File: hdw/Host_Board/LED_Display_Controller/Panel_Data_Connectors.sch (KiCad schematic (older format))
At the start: 4 parts

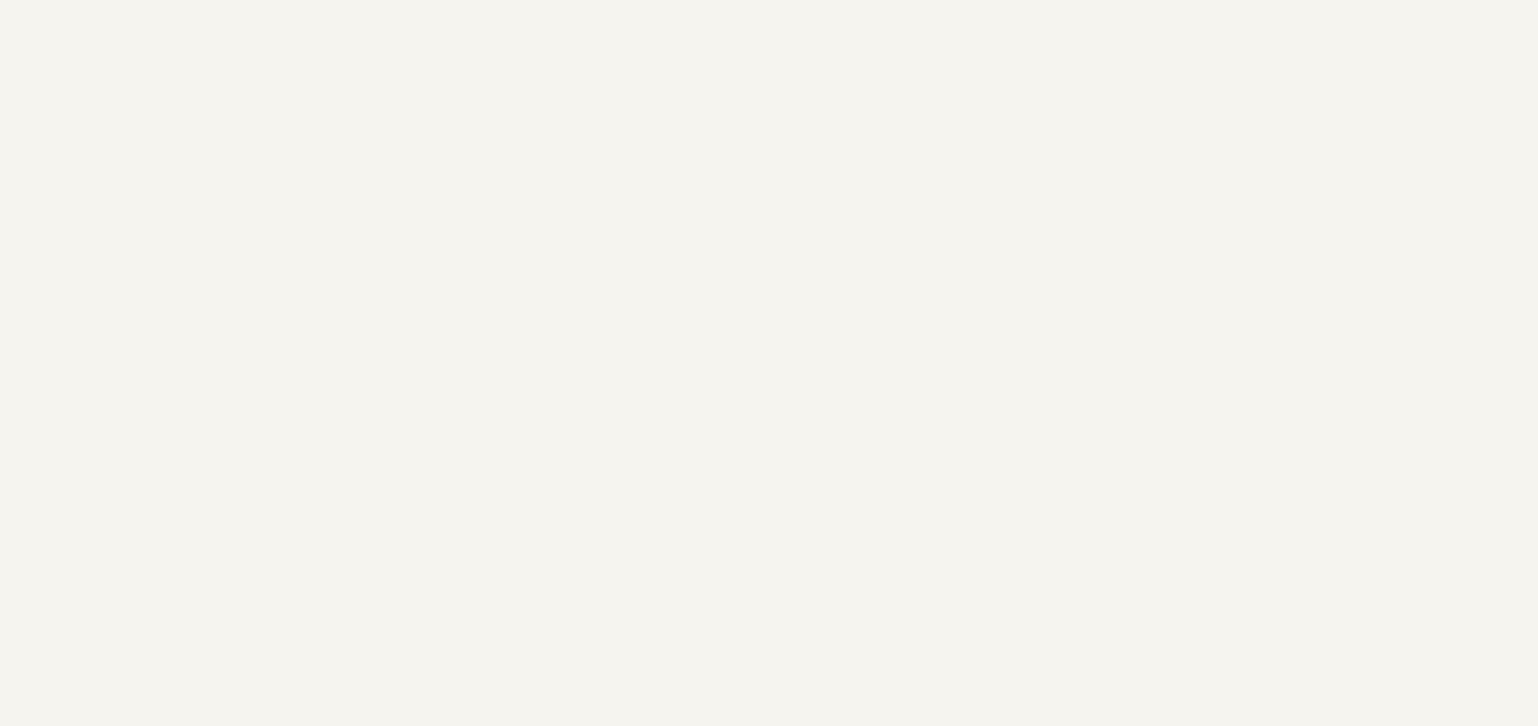
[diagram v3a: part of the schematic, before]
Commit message: Added graphical symbols to certain sheets
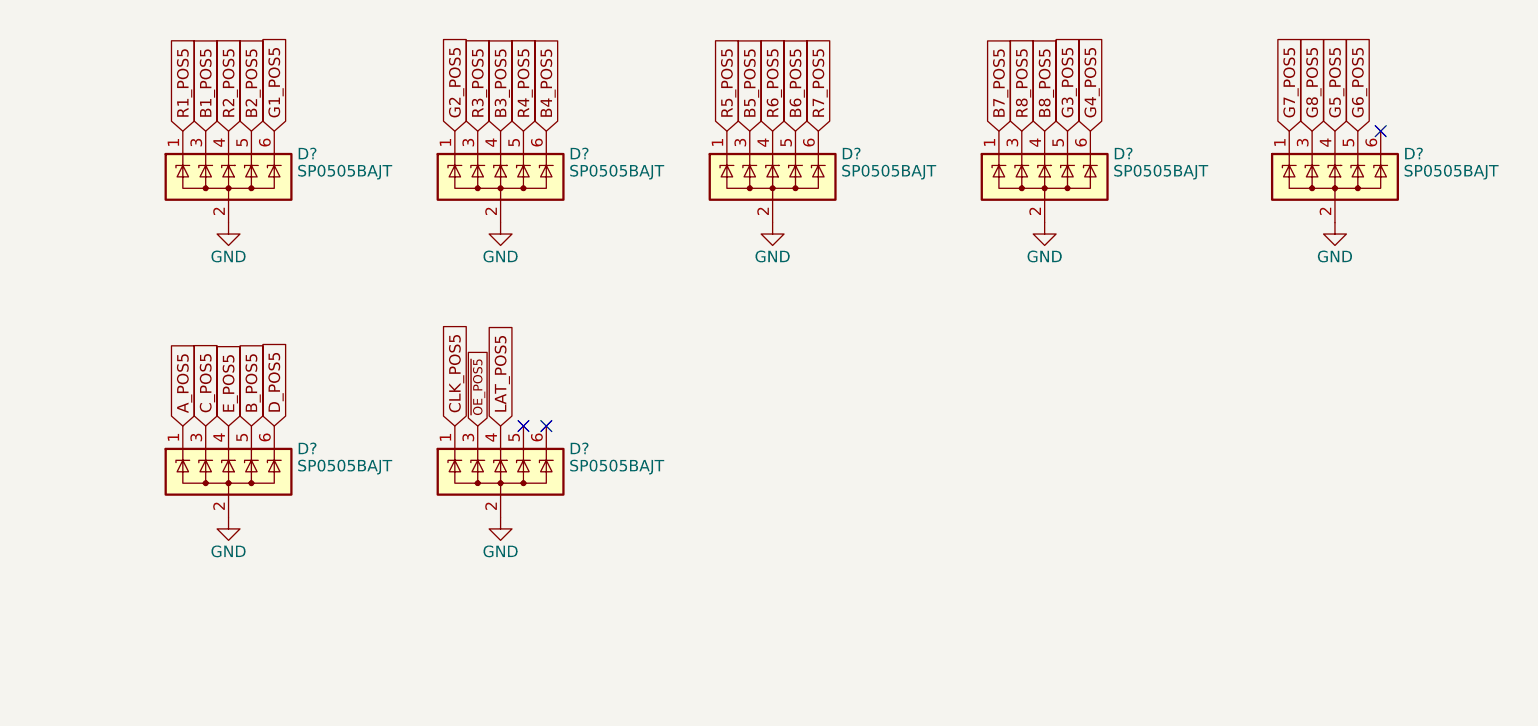
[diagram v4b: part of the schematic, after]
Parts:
- added D? (x7): SP0505BAJT, Package_TO_SOT_SMD:SOT-363_SC-70-6, symbol Power_Protection:SP0505BAJT
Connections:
- net A_POS5: now also D?.1 (K)
- net B1_POS5: now also D?.3 (K)
- net B2_POS5: now also D?.5 (K)
- net B3_POS5: now also D?.4 (K)
- net B4_POS5: now also D?.6 (K)
- net B5_POS5: now also D?.3 (K)
- net B6_POS5: now also D?.5 (K)
- net B7_POS5: now also D?.1 (K)
- net B8_POS5: now also D?.4 (K)
- net B_POS5: now also D?.5 (K)
- net CLK_POS5: now also D?.1 (K)
- net C_POS5: now also D?.3 (K)
- net D_POS5: now also D?.6 (K)
- net E_POS5: now also D?.4 (K)
- net G1_POS5: now also D?.6 (K)
- net G2_POS5: now also D?.1 (K)
- net G3_POS5: now also D?.5 (K)
- net G4_POS5: now also D?.6 (K)
- net G5_POS5: now also D?.4 (K)
- net G6_POS5: now also D?.5 (K)
- net G7_POS5: now also D?.1 (K)
- net G8_POS5: now also D?.3 (K)
- net GND: now also D?.2 (A), D?.2 (A), D?.2 (A), D?.2 (A), D?.2 (A), D?.2 (A), D?.2 (A)
- net LAT_POS5: now also D?.4 (K)
- net R1_POS5: now also D?.1 (K)
- net R2_POS5: now also D?.4 (K)
- net R3_POS5: now also D?.3 (K)
- net R4_POS5: now also D?.5 (K)
- net R5_POS5: now also D?.1 (K)
- net R6_POS5: now also D?.4 (K)
- net R7_POS5: now also D?.6 (K)
- net R8_POS5: now also D?.3 (K)
- net ~OE_POS5: now also D?.3 (K)
- no-connect marks 0 -> 3
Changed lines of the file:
@@
 	3400 6100 3400 6700
 Connection ~ 3400 6700
+$Comp
+L Power_Protection:SP0505BAJT D?
+U 1 1 5BFD0D17
+P 5000 1680
+F 0 "D?" H 5300 1780 50  0000 L CNN
+F 1 "SP0505BAJT" H 5300 1705 50  0000 L CNN
+F 2 "Package_TO_SOT_SMD:SOT-363_SC-70-6" H 5300 1630 50  0001 L CNN
+F 3 "http://www.littelfuse.com/~/media/files/littelfuse/technical%20resources/documents/data%20sheets/sp05xxba.pdf" H 5125 1805 50  0001 C CNN
+	1    5000 1680
+	1    0    0    -1
+$EndComp
+Text GLabel 4800 2770 1    50   Input ~ 0
+A_POS5
+Text GLabel 4900 2770 1    50   Input ~ 0
+C_POS5
+Text GLabel 4800 1480 1    50   Input ~ 0
+R1_POS5
+Text GLabel 4900 1480 1    50   Input ~ 0
+B1_POS5
+Text GLabel 5000 1480 1    50   Input ~ 0
+R2_POS5
+Text GLabel 5100 1480 1    50   Input ~ 0
+B2_POS5
+Text GLabel 5990 2770 1    50   Input ~ 0
+CLK_POS5
+Text GLabel 6090 2770 1    40   Input ~ 0
+~OE_POS5
+Text GLabel 5100 2770 1    50   Input ~ 0
+B_POS5
+Text GLabel 5200 2770 1    50   Input ~ 0
+D_POS5
+Text GLabel 5000 2770 1    50   Input ~ 0
+E_POS5
+Text GLabel 6190 2770 1    50   Input ~ 0
+LAT_POS5
+Text GLabel 5200 1480 1    50   Input ~ 0
+G1_POS5
+Text GLabel 5990 1480 1    50   Input ~ 0
+G2_POS5
+Text GLabel 6090 1480 1    50   Input ~ 0
+R3_POS5
+Text GLabel 6190 1480 1    50   Input ~ 0
+B3_POS5
+Text GLabel 6290 1480 1    50   Input ~ 0
+R4_POS5
+Text GLabel 6390 1480 1    50   Input ~ 0
+B4_POS5
+Text GLabel 7180 1480 1    50   Input ~ 0
+R5_POS5
+Text GLabel 7280 1480 1    50   Input ~ 0
+B5_POS5
+Text GLabel 7380 1480 1    50   Input ~ 0
+R6_POS5
+Text GLabel 7480 1480 1    50   Input ~ 0
+B6_POS5
+Text GLabel 7580 1480 1    50   Input ~ 0
+R7_POS5
+Text GLabel 8370 1480 1    50   Input ~ 0
+B7_POS5
+Text GLabel 8470 1480 1    50   Input ~ 0
+R8_POS5
+Text GLabel 8570 1480 1    50   Input ~ 0
+B8_POS5
+Text GLabel 8670 1480 1    50   Input ~ 0
+G3_POS5
+Text GLabel 8770 1480 1    50   Input ~ 0
+G4_POS5
+Text GLabel 9840 1480 1    50   Input ~ 0
+G5_POS5
+Text GLabel 9940 1480 1    50   Input ~ 0
+G6_POS5
+Text GLabel 9640 1480 1    50   Input ~ 0
+G7_POS5
+Text GLabel 9740 1480 1    50   Input ~ 0
+G8_POS5
+$Comp
+L power:GND #PWR?
+U 1 1 5BFE01B1
+P 5000 1880
+F 0 "#PWR?" H 5000 1630 50  0001 C CNN
+F 1 "GND" H 5000 1730 50  0000 C CNN
+F 2 "" H 5000 1880 50  0001 C CNN
+F 3 "" H 5000 1880 50  0001 C CNN
+	1    5000 1880
+	1    0    0    -1
+$EndComp
+$Comp
+L Power_Protection:SP0505BAJT D?
+U 1 1 5BFE2189
+P 6190 1680
+F 0 "D?" H 6490 1780 50  0000 L CNN
+F 1 "SP0505BAJT" H 6490 1705 50  0000 L CNN
+F 2 "Package_TO_SOT_SMD:SOT-363_SC-70-6" H 6490 1630 50  0001 L CNN
+F 3 "http://www.littelfuse.com/~/media/files/littelfuse/technical%20resources/documents/data%20sheets/sp05xxba.pdf" H 6315 1805 50  0001 C CNN
+	1    6190 1680
+	1    0    0    -1
+$EndComp
+$Comp
+L power:GND #PWR?
+U 1 1 5BFE2190
+P 6190 1880
+F 0 "#PWR?" H 6190 1630 50  0001 C CNN
+F 1 "GND" H 6190 1730 50  0000 C CNN
+F 2 "" H 6190 1880 50  0001 C CNN
+F 3 "" H 6190 1880 50  0001 C CNN
+	1    6190 1880
+	1    0    0    -1
+$EndComp
+$Comp
+L Power_Protection:SP0505BAJT D?
+U 1 1 5BFE454E
+P 7380 1680
+F 0 "D?" H 7680 1780 50  0000 L CNN
+F 1 "SP0505BAJT" H 7680 1705 50  0000 L CNN
+F 2 "Package_TO_SOT_SMD:SOT-363_SC-70-6" H 7680 1630 50  0001 L CNN
+F 3 "http://www.littelfuse.com/~/media/files/littelfuse/technical%20resources/documents/data%20sheets/sp05xxba.pdf" H 7505 1805 50  0001 C CNN
+	1    7380 1680
+	1    0    0    -1
+$EndComp
+$Comp
+L power:GND #PWR?
+U 1 1 5BFE4555
+P 7380 1880
+F 0 "#PWR?" H 7380 1630 50  0001 C CNN
+F 1 "GND" H 7380 1730 50  0000 C CNN
+F 2 "" H 7380 1880 50  0001 C CNN
+F 3 "" H 7380 1880 50  0001 C CNN
+	1    7380 1880
+	1    0    0    -1
+$EndComp
+$Comp
+L Power_Protection:SP0505BAJT D?
+U 1 1 5BFE8728
+P 8570 1680
+F 0 "D?" H 8870 1780 50  0000 L CNN
+F 1 "SP0505BAJT" H 8870 1705 50  0000 L CNN
+F 2 "Package_TO_SOT_SMD:SOT-363_SC-70-6" H 8870 1630 50  0001 L CNN
+F 3 "http://www.littelfuse.com/~/media/files/littelfuse/technical%20resources/documents/data%20sheets/sp05xxba.pdf" H 8695 1805 50  0001 C CNN
+	1    8570 1680
+	1    0    0    -1
+$EndComp
+$Comp
+L power:GND #PWR?
+U 1 1 5BFE872F
+P 8570 1880
+F 0 "#PWR?" H 8570 1630 50  0001 C CNN
+F 1 "GND" H 8570 1730 50  0000 C CNN
+F 2 "" H 8570 1880 50  0001 C CNN
+F 3 "" H 8570 1880 50  0001 C CNN
+	1    8570 1880
+	1    0    0    -1
+$EndComp
+$Comp
+L Power_Protection:SP0505BAJT D?
+U 1 1 5BFEC8F8
+P 5000 2970
+F 0 "D?" H 5300 3070 50  0000 L CNN
+F 1 "SP0505BAJT" H 5300 2995 50  0000 L CNN
+F 2 "Package_TO_SOT_SMD:SOT-363_SC-70-6" H 5300 2920 50  0001 L CNN
+F 3 "http://www.littelfuse.com/~/media/files/littelfuse/technical%20resources/documents/data%20sheets/sp05xxba.pdf" H 5125 3095 50  0001 C CNN
+	1    5000 2970
+	1    0    0    -1
+$EndComp
+$Comp
+L power:GND #PWR?
+U 1 1 5BFEC8FF
+P 5000 3170
+F 0 "#PWR?" H 5000 2920 50  0001 C CNN
+F 1 "GND" H 5000 3020 50  0000 C CNN
+F 2 "" H 5000 3170 50  0001 C CNN
+F 3 "" H 5000 3170 50  0001 C CNN
+	1    5000 3170
+	1    0    0    -1
+$EndComp
+$Comp
+L Power_Protection:SP0505BAJT D?
+U 1 1 5BFEEC83
+P 6190 2970
+F 0 "D?" H 6490 3070 50  0000 L CNN
+F 1 "SP0505BAJT" H 6490 2995 50  0000 L CNN
+F 2 "Package_TO_SOT_SMD:SOT-363_SC-70-6" H 6490 2920 50  0001 L CNN
+F 3 "http://www.littelfuse.com/~/media/files/littelfuse/technical%20resources/documents/data%20sheets/sp05xxba.pdf" H 6315 3095 50  0001 C CNN
+	1    6190 2970
+	1    0    0    -1
+$EndComp
+$Comp
+L power:GND #PWR?
+U 1 1 5BFEEC8A
+P 6190 3170
+F 0 "#PWR?" H 6190 2920 50  0001 C CNN
+F 1 "GND" H 6190 3020 50  0000 C CNN
+F 2 "" H 6190 3170 50  0001 C CNN
+F 3 "" H 6190 3170 50  0001 C CNN
+	1    6190 3170
+	1    0    0    -1
+$EndComp
+$Comp
+L Power_Protection:SP0505BAJT D?
+U 1 1 5BFF32EE
+P 9840 1680
+F 0 "D?" H 10140 1780 50  0000 L CNN
+F 1 "SP0505BAJT" H 10140 1705 50  0000 L CNN
+F 2 "Package_TO_SOT_SMD:SOT-363_SC-70-6" H 10140 1630 50  0001 L CNN
+F 3 "http://www.littelfuse.com/~/media/files/littelfuse/technical%20resources/documents/data%20sheets/sp05xxba.pdf" H 9965 1805 50  0001 C CNN
+	1    9840 1680
+	1    0    0    -1
+$EndComp
+$Comp
+L power:GND #PWR?
+U 1 1 5BFF32F5
+P 9840 1880
+F 0 "#PWR?" H 9840 1630 50  0001 C CNN
+F 1 "GND" H 9840 1730 50  0000 C CNN
+F 2 "" H 9840 1880 50  0001 C CNN
+F 3 "" H 9840 1880 50  0001 C CNN
+	1    9840 1880
+	1    0    0    -1
+$EndComp
+NoConn ~ 10040 1480
+NoConn ~ 6290 2770
+NoConn ~ 6390 2770
 $EndSCHEMATC

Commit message: Cleaned up a few sheets
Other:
- note added: "String 1 is the top string,\nString 4 is the bottom string.\nEach string is 5 panels long\nEach panel is 64x64 pixels\nThis yields a 320x256 pixel overall display resolution"
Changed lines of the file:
@@
 NoConn ~ 6290 2770
 NoConn ~ 6390 2770
+Text Notes 6710 5650 0    50   ~ 0
+String 1 is the top string,\nString 4 is the bottom string.\nEach string is 5 panels long\nEach panel is 64x64 pixels\nThis yields a 320x256 pixel overall display resolution
 $EndSCHEMATC

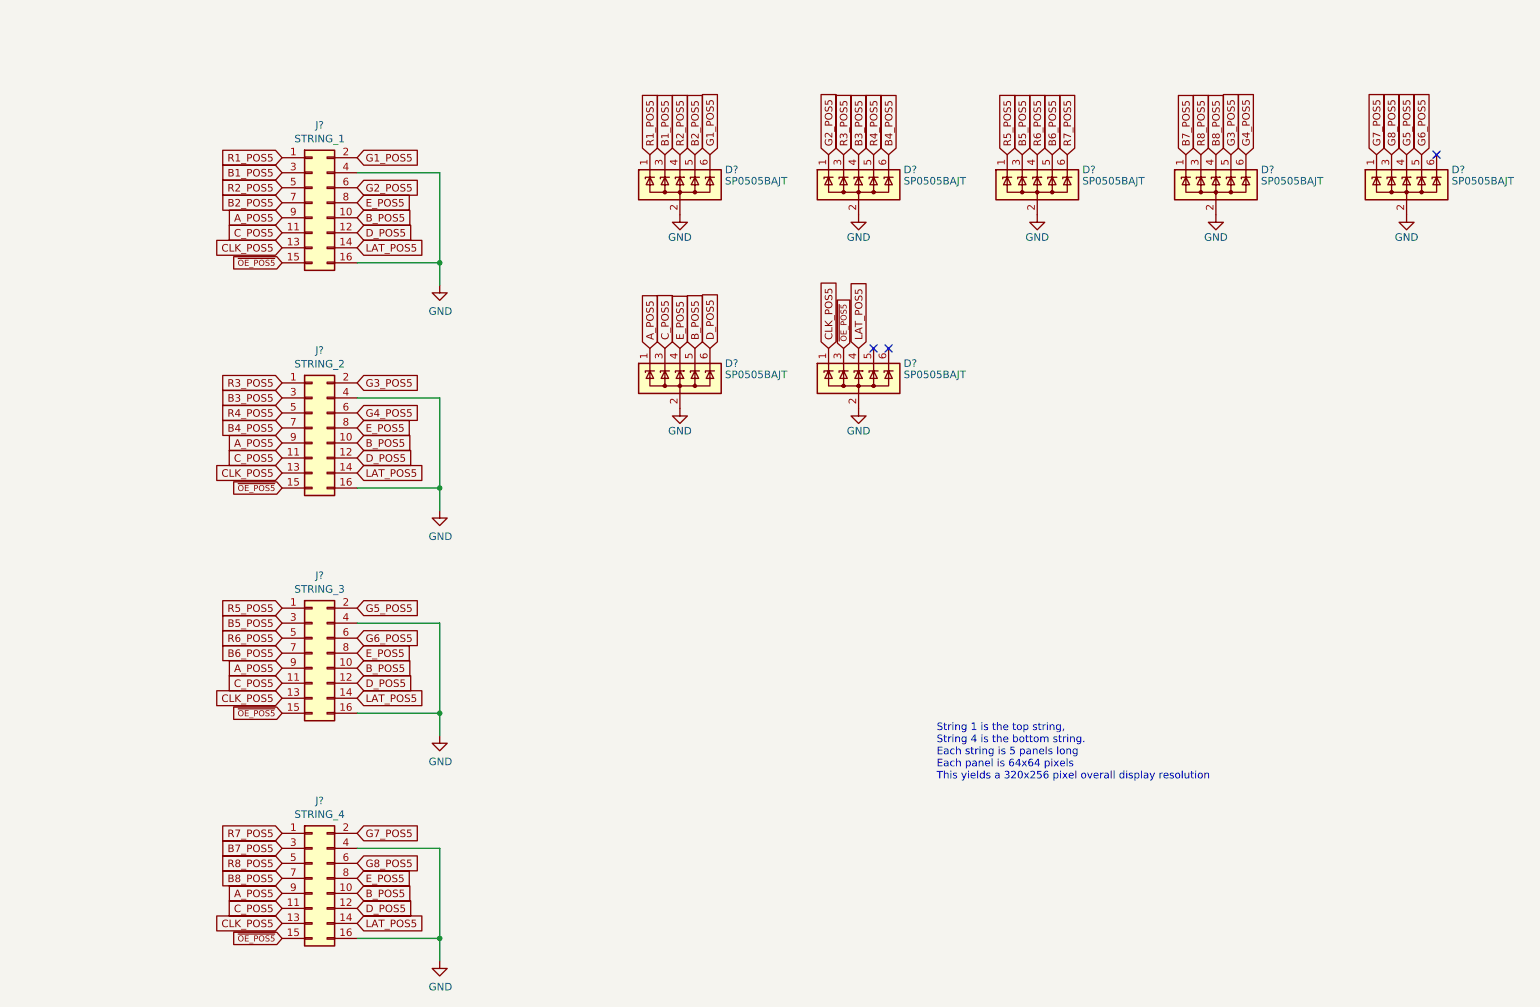
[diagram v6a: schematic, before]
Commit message: Added titles and MU logo to each sheet
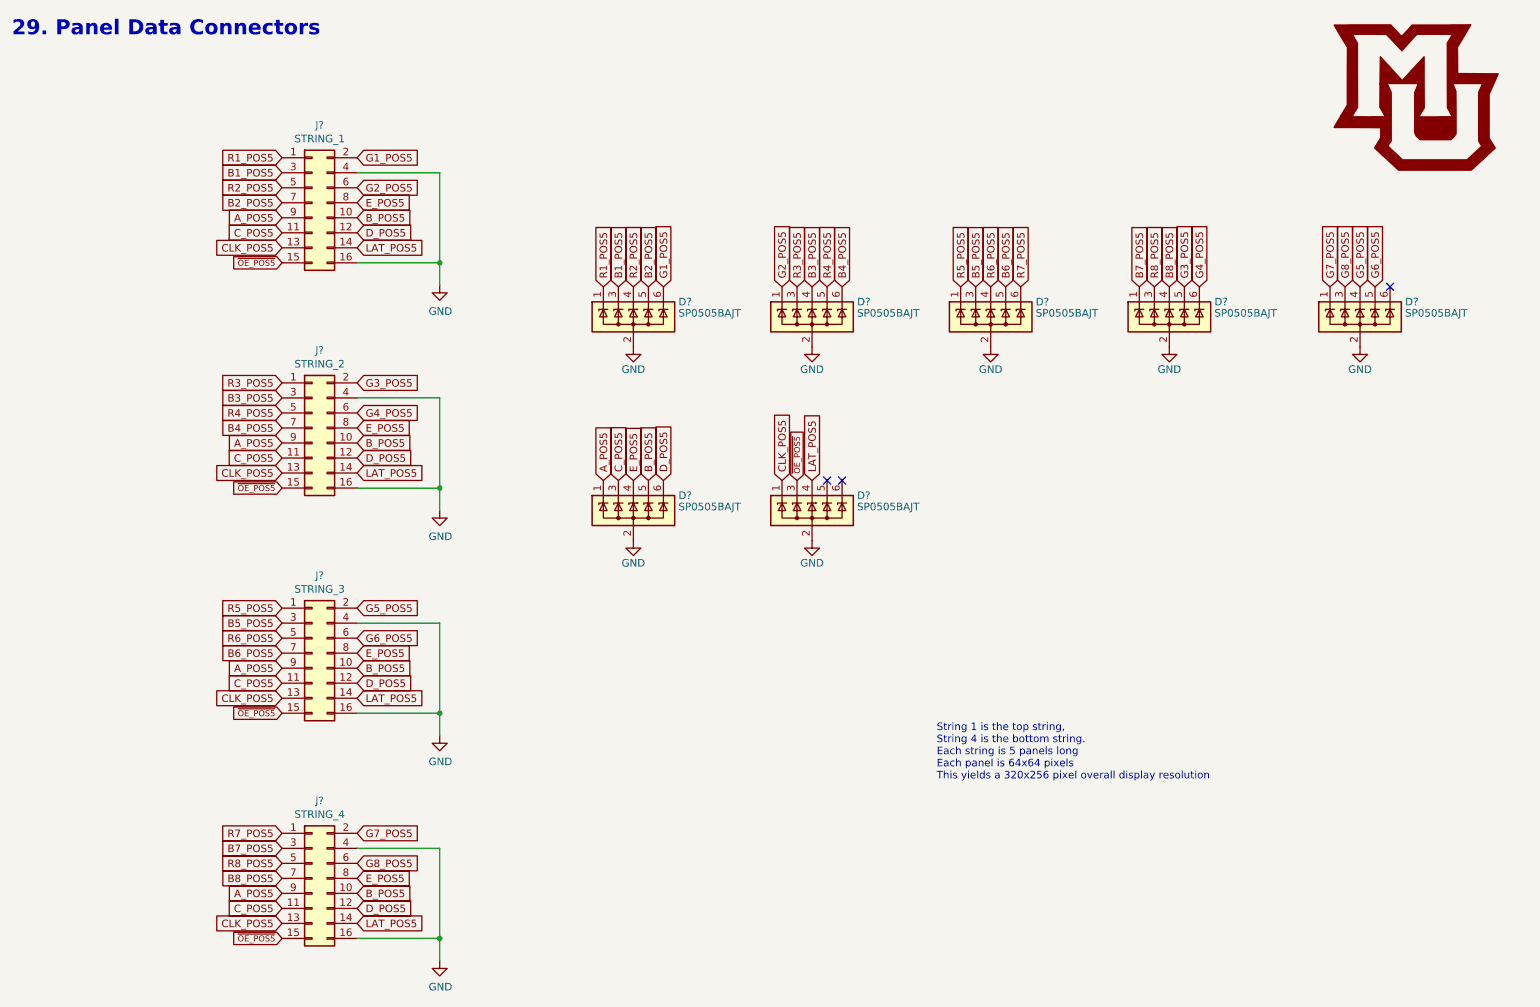
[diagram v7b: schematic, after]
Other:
- note added: "29. Panel Data Connectors"
- moved on the sheet: D?
